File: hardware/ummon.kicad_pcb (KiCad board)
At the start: 4 copper layers, 125 x 80 mm, 86 parts, among them J1 Conn_01x08_Pin, J2 Conn_01x05_Pin, J3 Conn_01x04_Pin, J4 Conn_01x04_Pin, J5 Conn_01x04_Pin, P1 FPC 0.5MM 24P Vertical, Q1 SI1308EDL, SW1 Reboot, SW2 Flash, SW3 Test Button, U1 ESP32-C6-WROOM-1-N8, U2 SCD41-D-R2, U3 SGP41-D-R4, U4 SHT41-AD1B-R2, U5 AMS1117-3.3, U7 SMBJ6.5CA

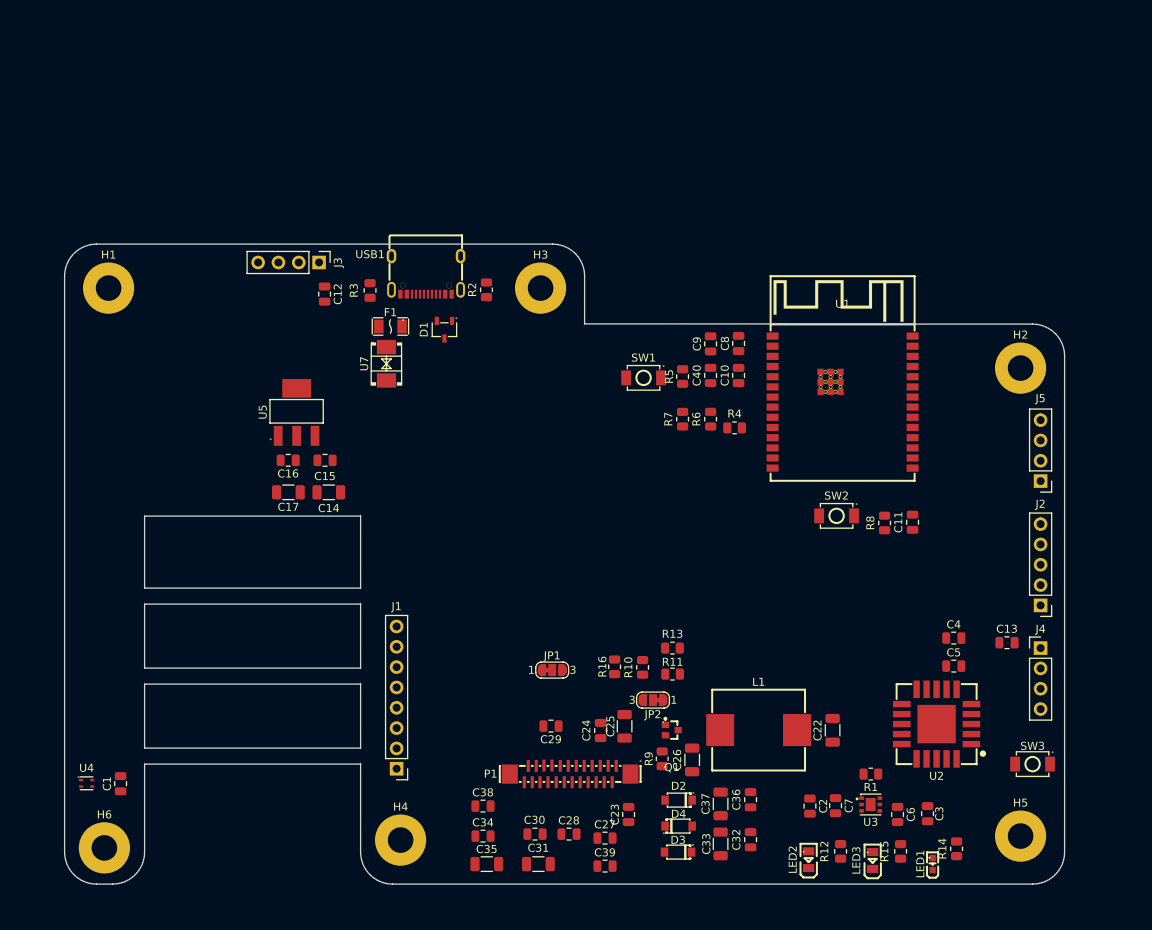
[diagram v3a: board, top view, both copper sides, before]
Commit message: :sparkles: Power routing
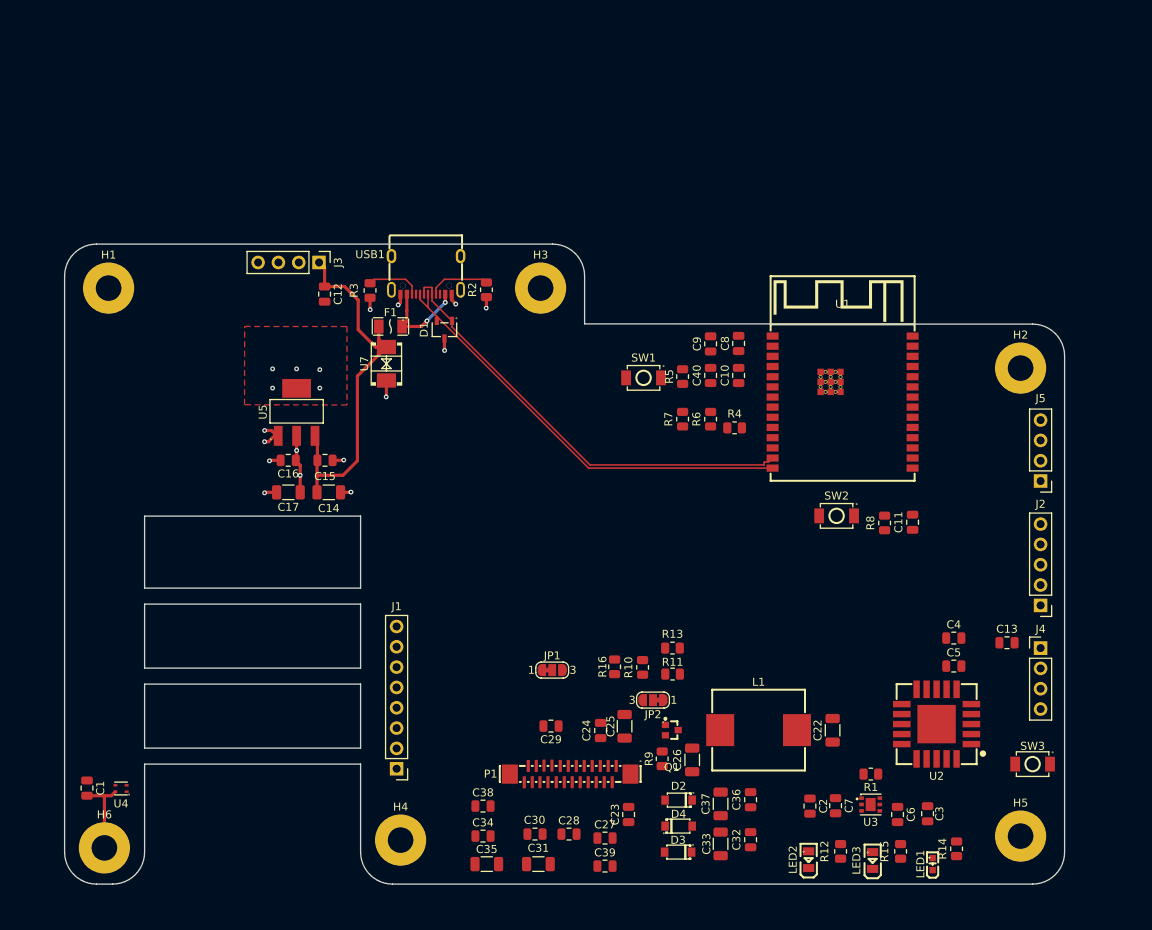
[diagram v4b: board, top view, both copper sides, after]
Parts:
- moved U4 4.35 mm to (57.0, 138.1), turned to 180 degrees
- moved C1 4.24 mm to (52.8, 138.0), turned to -90 degrees
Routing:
- net /USB_D+: track 0.00 -> 55.7 mm
- net /USB_D-: track 0.00 -> 55.6 mm
- net GND: track 0.00 -> 49.3 mm, vias 0 -> 12
- net +5V: track 0.00 -> 48.0 mm
- net Net-(F1-Pad1): track 0.00 -> 12.1 mm, vias 0 -> 2
- net Net-(USB1-CC1): track 0.00 -> 7.70 mm
- net +3.3V: track 0.00 -> 7.33 mm, vias 0 -> 7
- net Net-(USB1-CC2): track 0.00 -> 6.83 mm
- added copper zone on F.Cu, net +3.3V

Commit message: :sparkles: Completes Routing
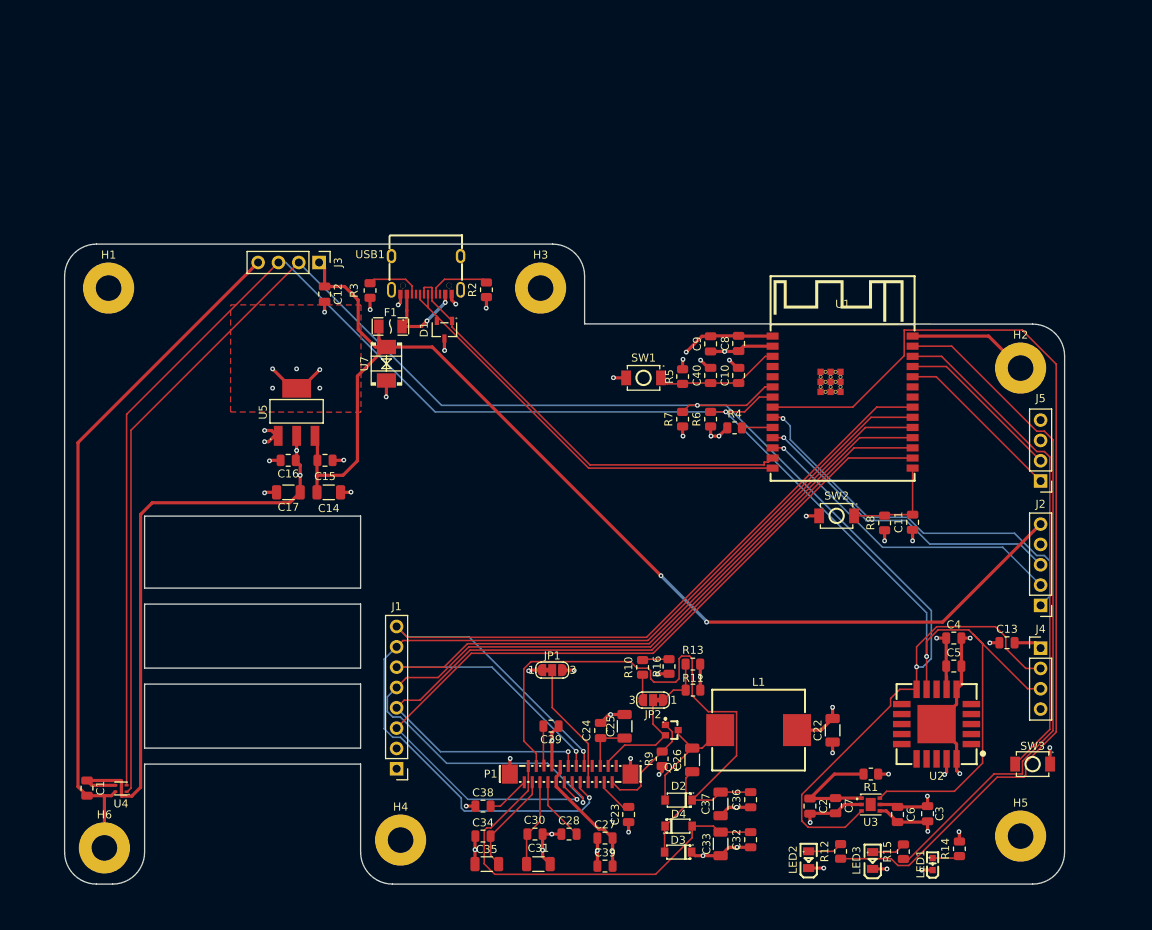
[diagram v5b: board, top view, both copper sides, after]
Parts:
- moved R16 6.80 mm to (125.5, 122.8)
- moved R11 3.24 mm to (128.6, 125.8)
- moved R13 3.24 mm to (128.5, 122.5)
- moved R15 0.35 mm to (154.8, 145.9)
- moved R14 0.35 mm to (161.8, 145.6)
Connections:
- U1 pad : (no net) -> GND
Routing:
- net /I2C_SDA: track 0.00 -> 250.2 mm, vias 0 -> 2
- net /I2C_SCL: track 0.00 -> 241.5 mm, vias 0 -> 2
- net GND: track 49.3 -> 256.6 mm, vias 12 -> 47
- net +3.3V: track 7.33 -> 147.5 mm, vias 7 -> 21
- net /GPIO0: track 0.00 -> 124.2 mm
- net /EPD_RST: track 0.00 -> 121.4 mm, vias 0 -> 1
- net /EPD_CS: track 0.00 -> 113.5 mm, vias 0 -> 1
- net /EPD_BUSY: track 0.00 -> 108.7 mm, vias 0 -> 1
- net /EPD_DIN: track 0.00 -> 107.5 mm, vias 0 -> 1
- net /EPD_DC: track 0.00 -> 105.6 mm, vias 0 -> 1
- net /EPD_SCK: track 0.00 -> 103.5 mm, vias 0 -> 1
- net +5V: track 48.0 -> 149.2 mm, vias 0 -> 2
- net /GPIO2: track 0.00 -> 85.0 mm
- net /EPD_PREVGH: track 0.00 -> 70.9 mm
- net /GPIO3: track 0.00 -> 62.5 mm
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
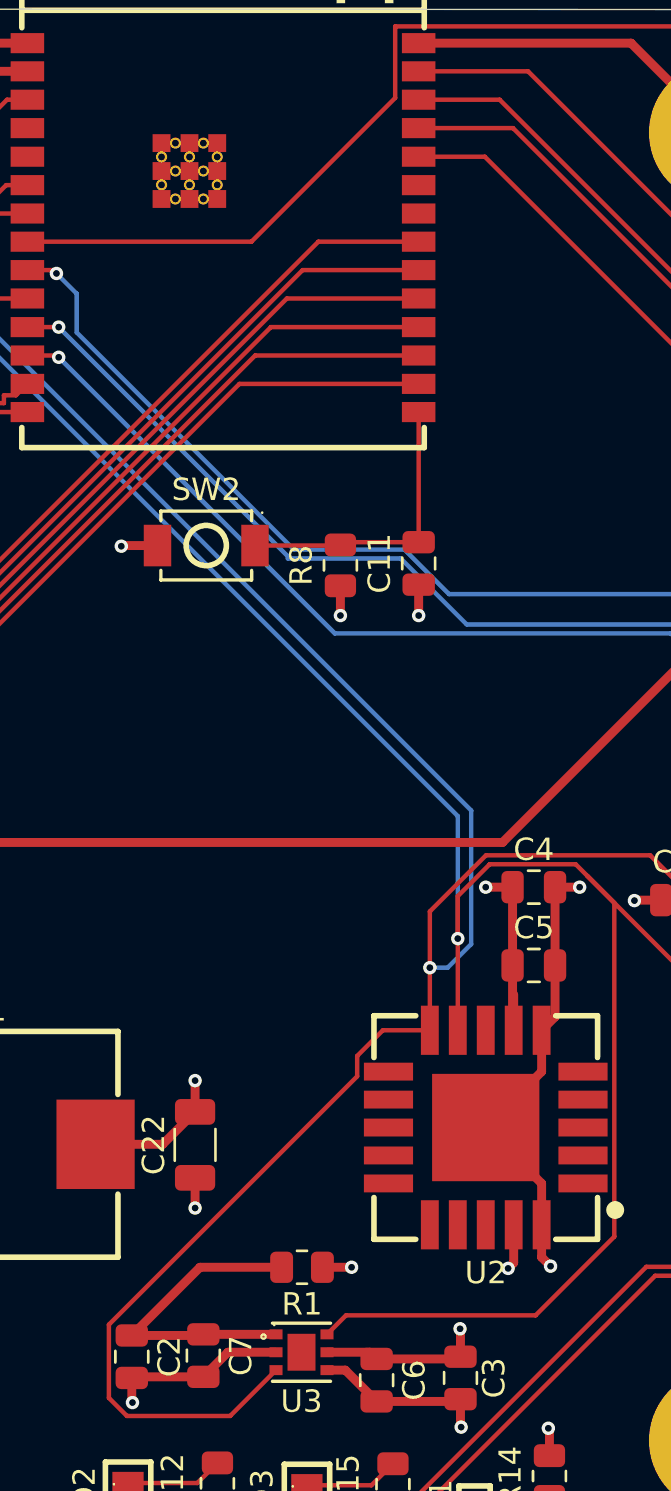
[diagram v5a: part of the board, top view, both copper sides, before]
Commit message: :sparkles: ESP via fixes
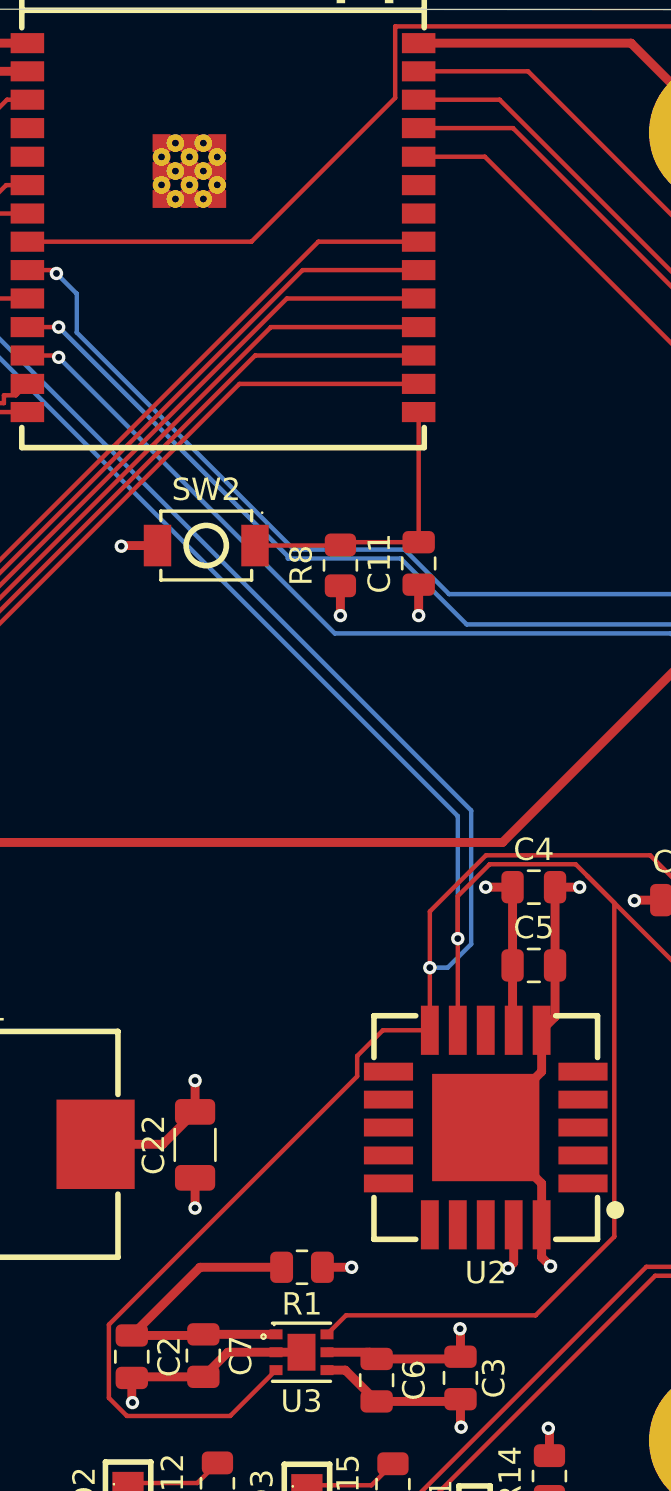
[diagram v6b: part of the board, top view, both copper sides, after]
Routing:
- net +3.3V: track 147.5 -> 145.9 mm
- net GND: track 256.6 -> 257.8 mm
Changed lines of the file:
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@@
 		(pad "" thru_hole circle
 			(at -2.75 -3.16)
-			(size 0.5 0.5)
+			(size 0.8 0.5)
 			(drill 0.3)
 			(layers "*.Cu" "*.Paste" "*.Mask")
@@
 		(pad "" thru_hole circle
 			(at -2.75 -1.91)
-			(size 0.5 0.5)
+			(size 0.8 0.5)
 			(drill 0.3)
 			(layers "*.Cu" "*.Paste" "*.Mask")
@@
 		(pad "" thru_hole circle
 			(at -2.13 -3.78)
-			(size 0.5 0.5)
+			(size 0.8 0.5)
 			(drill 0.3)
 			(layers "*.Cu" "*.Paste" "*.Mask")
@@
 		(pad "" thru_hole circle
 			(at -2.13 -2.53)
-			(size 0.5 0.5)
+			(size 0.8 0.5)
 			(drill 0.3)
 			(layers "*.Cu" "*.Paste" "*.Mask")
@@
 		(pad "" thru_hole circle
 			(at -2.13 -1.28)
-			(size 0.5 0.5)
+			(size 0.8 0.5)
 			(drill 0.3)
 			(layers "*.Cu" "*.Paste" "*.Mask")
@@
 		(pad "" thru_hole circle
 			(at -1.5 -3.16)
-			(size 0.5 0.5)
+			(size 0.8 0.5)
 			(drill 0.3)
 			(layers "*.Cu" "*.Paste" "*.Mask")
@@
 		(pad "" thru_hole circle
 			(at -1.5 -1.91)
-			(size 0.5 0.5)
+			(size 0.8 0.5)
 			(drill 0.3)
 			(layers "*.Cu" "*.Paste" "*.Mask")
@@
 		(pad "" thru_hole circle
 			(at -0.88 -3.78)
-			(size 0.5 0.5)
+			(size 0.8 0.5)
 			(drill 0.3)
 			(layers "*.Cu" "*.Paste" "*.Mask")
@@
 		(pad "" thru_hole circle
 			(at -0.88 -2.53)
-			(size 0.5 0.5)
+			(size 0.8 0.5)
 			(drill 0.3)
 			(layers "*.Cu" "*.Paste" "*.Mask")
@@
 		(pad "" thru_hole circle
 			(at -0.88 -1.28)
-			(size 0.5 0.5)
+			(size 0.8 0.5)
 			(drill 0.3)
 			(layers "*.Cu" "*.Paste" "*.Mask")
@@
 		(pad "" thru_hole circle
 			(at -0.26 -3.16)
-			(size 0.5 0.5)
+			(size 0.8 0.5)
 			(drill 0.3)
 			(layers "*.Cu" "*.Paste" "*.Mask")
@@
 		(pad "" thru_hole circle
 			(at -0.26 -1.91)
-			(size 0.5 0.5)
+			(size 0.8 0.5)
 			(drill 0.3)
 			(layers "*.Cu" "*.Paste" "*.Mask")
@@
 	)
 	(segment
+		(start 149.62 140.05)
+		(end 150.76 140.05)
+		(width 0.4)
+		(layer "F.Cu")
+		(net "GND")
+	)
+	(segment
 		(start 90.23 87.0475)
 		(end 90.23 89.07)
@@
 		(width 0.4)
 		(layer "F.Cu")
-		(net "+3.3V")
-	)
-	(segment
-		(start 160.25 125.65)
-		(end 160.25 124.05)
-		(width 0.4)
-		(layer "F.Cu")

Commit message: :sparkles: Add gnd plane on top layer
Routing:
- net GND: vias 47 -> 81
- added copper zone on F.Cu, net GND

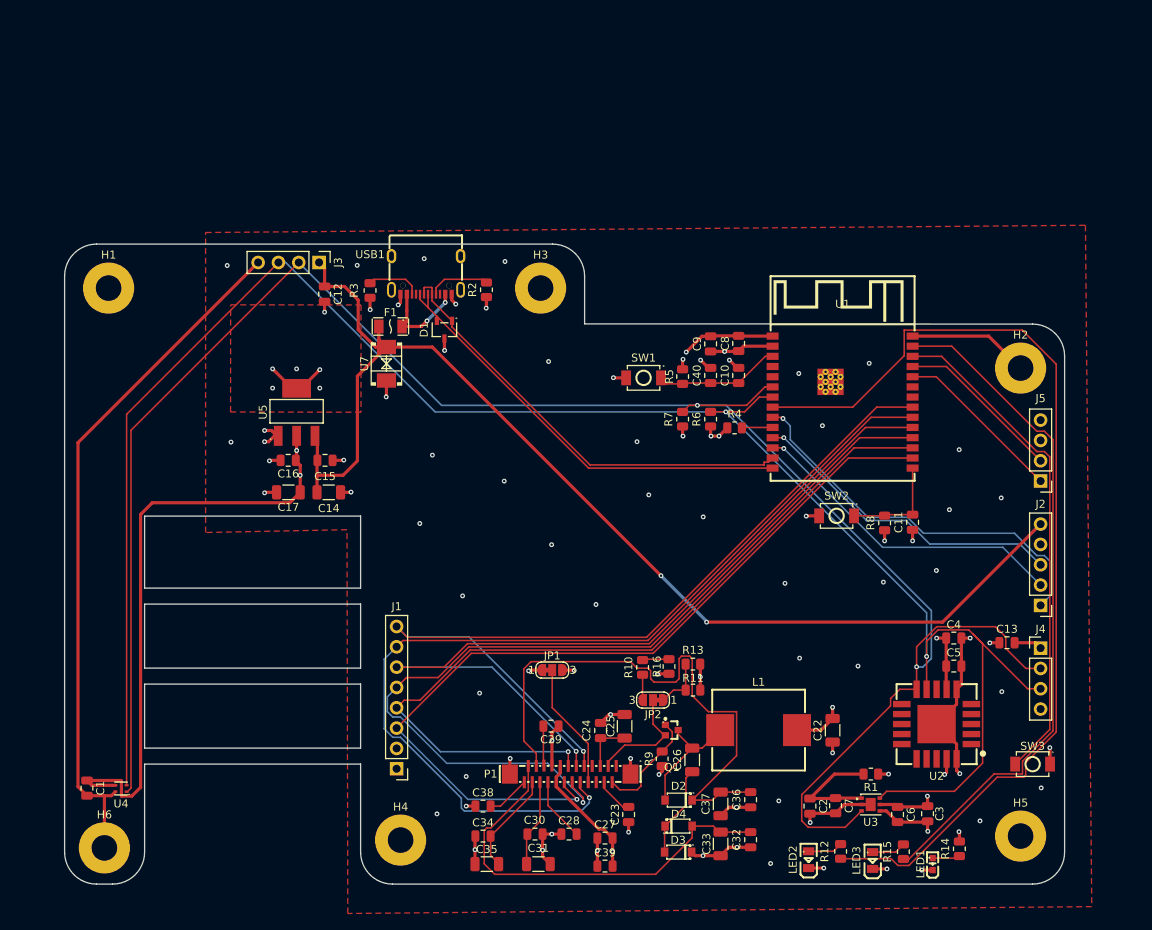
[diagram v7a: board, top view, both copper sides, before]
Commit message: :zap: Differential routing of USB_DATA
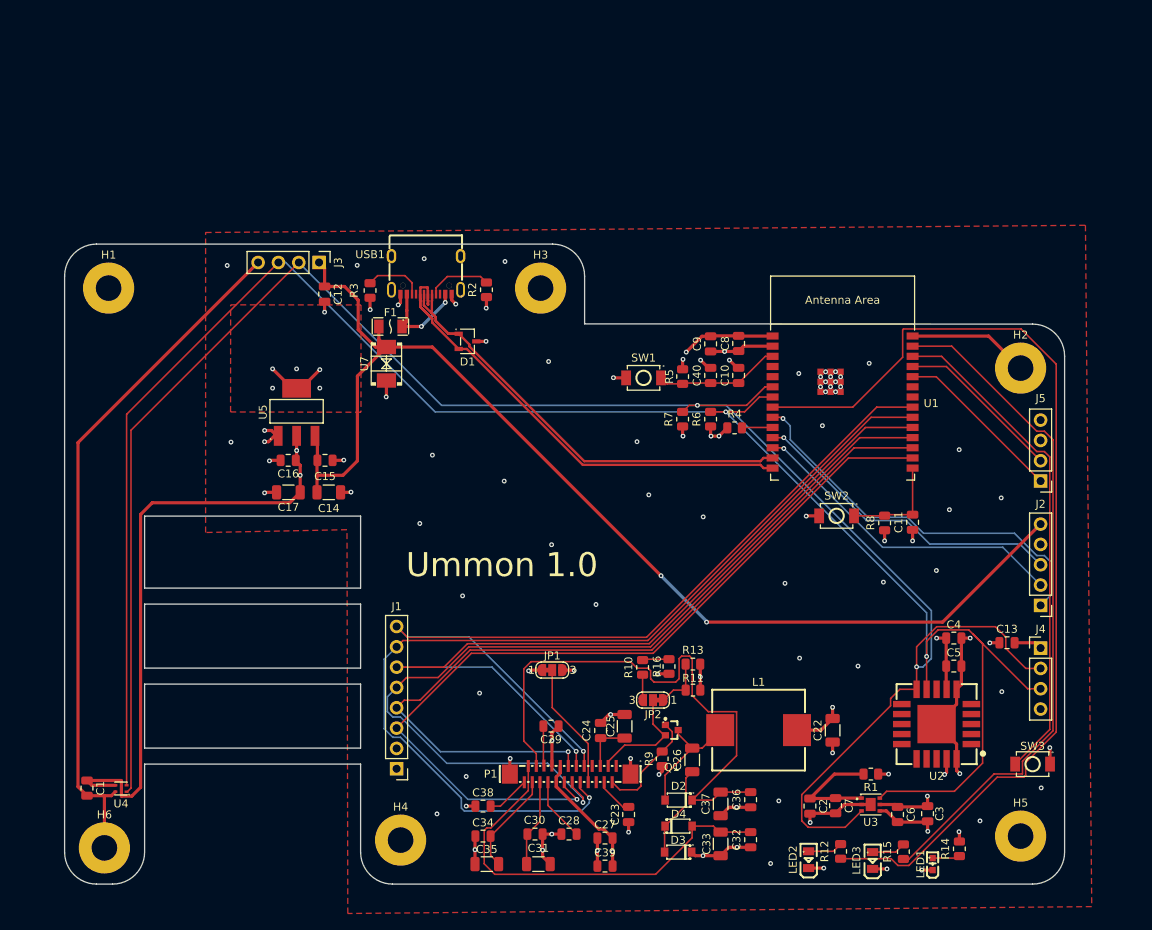
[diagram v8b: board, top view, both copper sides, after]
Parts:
- U1: footprint parts:WIRELM-SMD_ESP32-C6-WROOM-1 -> PCM_Espressif:ESP32-C6-WROOM-1
- moved D1 3.23 mm to (100.4, 82.2), turned to 180 degrees
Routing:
- net /USB_D+: track 55.7 -> 63.2 mm
- net /USB_D-: track 55.6 -> 60.7 mm
- net Net-(USB1-CC2): track 6.83 -> 7.44 mm
- net GND: track 257.8 -> 257.5 mm, vias 81 -> 92
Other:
- board text added: "Ummon 1.0"
